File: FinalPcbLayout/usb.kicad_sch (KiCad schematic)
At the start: 1 part, among them J5 USB_C_Receptacle

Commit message: sound chip done
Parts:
- added R8, R9: 5.1k, symbol Device:R
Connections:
- net GND1: now reaches J5.A1 (GND), J5.A12 (GND), J5.B1 (GND), J5.B12 (GND)
- net VCC: now reaches J5.A4 (VBUS), J5.A9 (VBUS), J5.B4 (VBUS), J5.B9 (VBUS)
- net at J5.A5 (CC1): now also R9.1
- net D+1: now reaches J5.A6 (D+)
- net D+1: now also J5.B7 (D-)
- net D-1: now reaches J5.A7 (D-)
- net D-1: now also J5.B6 (D+)
- net at J5.B5 (CC2): now also R8.1
- net GND: now reaches J5.S1 (SHIELD)
- net GND: now also R8.2, R9.2
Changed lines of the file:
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@@
 (kicad_sch (version 20230121) (generator eeschema)
   (paper "A4")
+  (wire (pts (xy 157.48 68.58) (xy 209.55 68.58))
+    (stroke (width 0) (type default))
+  )
+  (wire (pts (xy 157.48 78.74) (xy 162.56 78.74))
+    (stroke (width 0) (type default))
+  )
+  (wire (pts (xy 209.55 68.58) (xy 209.55 69.85))
+    (stroke (width 0) (type default))
+  )
+  (wire (pts (xy 157.48 83.82) (xy 170.18 83.82))
+    (stroke (width 0) (type default))
+  )
+  (wire (pts (xy 162.56 81.28) (xy 157.48 81.28))
+    (stroke (width 0) (type default))
+  )
+  (wire (pts (xy 170.18 76.2) (xy 157.48 76.2))
+    (stroke (width 0) (type default))
+  )
+  (wire (pts (xy 170.18 83.82) (xy 170.18 76.2))
+    (stroke (width 0) (type default))
+  )
+  (wire (pts (xy 162.56 78.74) (xy 162.56 81.28))
+    (stroke (width 0) (type default))
+  )
+  (wire (pts (xy 157.48 71.12) (xy 187.96 71.12))
+    (stroke (width 0) (type default))
+  )
+  (hierarchical_label "D+1" (shape input) (at 162.56 81.28 0) (fields_autoplaced)
+    (effects (font (size 1.27 1.27)) (justify left))
+  )
+  (hierarchical_label "GND1" (shape input) (at 142.24 129.54 270) (fields_autoplaced)
+    (effects (font (size 1.27 1.27)) (justify right))
+  )
+  (hierarchical_label "VCC" (shape input) (at 157.48 63.5 0) (fields_autoplaced)
+    (effects (font (size 1.27 1.27)) (justify left))
+  )
+  (hierarchical_label "D-1" (shape input) (at 170.18 76.2 0) (fields_autoplaced)
+    (effects (font (size 1.27 1.27)) (justify left))
+  )
+  (symbol (lib_id "power:GND") (at 187.96 78.74 0) (unit 1)
+    (in_bom yes) (on_board yes) (dnp no) (fields_autoplaced)
+    (property "Reference" "#PWR027" (at 187.96 85.09 0)
+      (effects (font (size 1.27 1.27)) hide)
+    )
+    (property "Value" "GND" (at 187.96 83.82 0)
+      (effects (font (size 1.27 1.27)))
+    )
+    (property "Footprint" "" (at 187.96 78.74 0)
+      (effects (font (size 1.27 1.27)) hide)
+    )
+    (property "Datasheet" "" (at 187.96 78.74 0)
+      (effects (font (size 1.27 1.27)) hide)
+    )
+    (pin "1")
+    (instances
+      (project "FinalPcbLayout"
+        (path "/9fcc273e-b318-4ade-b4c7-fe4ddbf9d677/80fb5872-9ff7-41e5-9921-84d432e9852e"
+          (reference "#PWR027") (unit 1)
+        )
+      )
+    )
+  )
+  (symbol (lib_id "Device:R") (at 209.55 73.66 0) (unit 1)
+    (in_bom yes) (on_board yes) (dnp no) (fields_autoplaced)
+    (property "Reference" "R9" (at 212.09 72.39 0)
+      (effects (font (size 1.27 1.27)) (justify left))
+    )
+    (property "Value" "5.1k" (at 212.09 74.93 0)
+      (effects (font (size 1.27 1.27)) (justify left))
+    )
+    (property "Footprint" "" (at 207.772 73.66 90)
+      (effects (font (size 1.27 1.27)) hide)
+    )
+    (property "Datasheet" "~" (at 209.55 73.66 0)
+      (effects (font (size 1.27 1.27)) hide)
+    )
+    (pin "1")
+    (pin "2")
+    (instances
+      (project "FinalPcbLayout"
+        (path "/9fcc273e-b318-4ade-b4c7-fe4ddbf9d677/80fb5872-9ff7-41e5-9921-84d432e9852e"
+          (reference "R9") (unit 1)
+        )
+      )
+    )
+  )
+  (symbol (lib_id "power:GND") (at 209.55 77.47 0) (unit 1)
+    (in_bom yes) (on_board yes) (dnp no) (fields_autoplaced)
+    (property "Reference" "#PWR028" (at 209.55 83.82 0)
+      (effects (font (size 1.27 1.27)) hide)
+    )
+    (property "Value" "GND" (at 209.55 82.55 0)
+      (effects (font (size 1.27 1.27)))
+    )
+    (property "Footprint" "" (at 209.55 77.47 0)
+      (effects (font (size 1.27 1.27)) hide)
+    )
+    (property "Datasheet" "" (at 209.55 77.47 0)
+      (effects (font (size 1.27 1.27)) hide)
+    )
+    (pin "1")
+    (instances
+      (project "FinalPcbLayout"
+        (path "/9fcc273e-b318-4ade-b4c7-fe4ddbf9d677/80fb5872-9ff7-41e5-9921-84d432e9852e"
+          (reference "#PWR028") (unit 1)
+        )
+      )
+    )
+  )
+  (symbol (lib_id "power:GND") (at 134.62 129.54 0) (unit 1)
+    (in_bom yes) (on_board yes) (dnp no) (fields_autoplaced)
+    (property "Reference" "#PWR07" (at 134.62 135.89 0)
+      (effects (font (size 1.27 1.27)) hide)
+    )
+    (property "Value" "GND" (at 134.62 134.62 0)
+      (effects (font (size 1.27 1.27)))
+    )
+    (property "Footprint" "" (at 134.62 129.54 0)
+      (effects (font (size 1.27 1.27)) hide)
+    )
+    (property "Datasheet" "" (at 134.62 129.54 0)
+      (effects (font (size 1.27 1.27)) hide)
+    )
+    (pin "1")
+    (instances
+      (project "FinalPcbLayout"
+        (path "/9fcc273e-b318-4ade-b4c7-fe4ddbf9d677/80fb5872-9ff7-41e5-9921-84d432e9852e"
+          (reference "#PWR07") (unit 1)
+        )
+      )
+    )
+  )
+  (symbol (lib_id "Device:R") (at 187.96 74.93 0) (unit 1)
+    (in_bom yes) (on_board yes) (dnp no) (fields_autoplaced)
+    (property "Reference" "R8" (at 190.5 73.66 0)
+      (effects (font (size 1.27 1.27)) (justify left))
+    )
+    (property "Value" "5.1k" (at 190.5 76.2 0)
+      (effects (font (size 1.27 1.27)) (justify left))
+    )
+    (property "Footprint" "" (at 186.182 74.93 90)
+      (effects (font (size 1.27 1.27)) hide)
+    )
+    (property "Datasheet" "~" (at 187.96 74.93 0)
+      (effects (font (size 1.27 1.27)) hide)
+    )
+    (pin "1")
+    (pin "2")
+    (instances
+      (project "FinalPcbLayout"
+        (path "/9fcc273e-b318-4ade-b4c7-fe4ddbf9d677/80fb5872-9ff7-41e5-9921-84d432e9852e"
+          (reference "R8") (unit 1)
+        )
+      )
+    )
+  )
   (symbol (lib_id "Connector:USB_C_Receptacle") (at 142.24 88.9 0) (unit 1)
     (in_bom yes) (on_board yes) (dnp no) (fields_autoplaced)

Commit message: beep
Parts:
- added U6: CP2102N-Axx-xQFN28, Package_DFN_QFN:QFN-28-1EP_5x5mm_P0.5mm_EP3.35x3.35mm, symbol Interface_USB:CP2102N-Axx-xQFN28
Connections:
- new net: U6.29 (GND), U6.3 (GND)
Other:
- moved on the sheet: J5, R8, R9

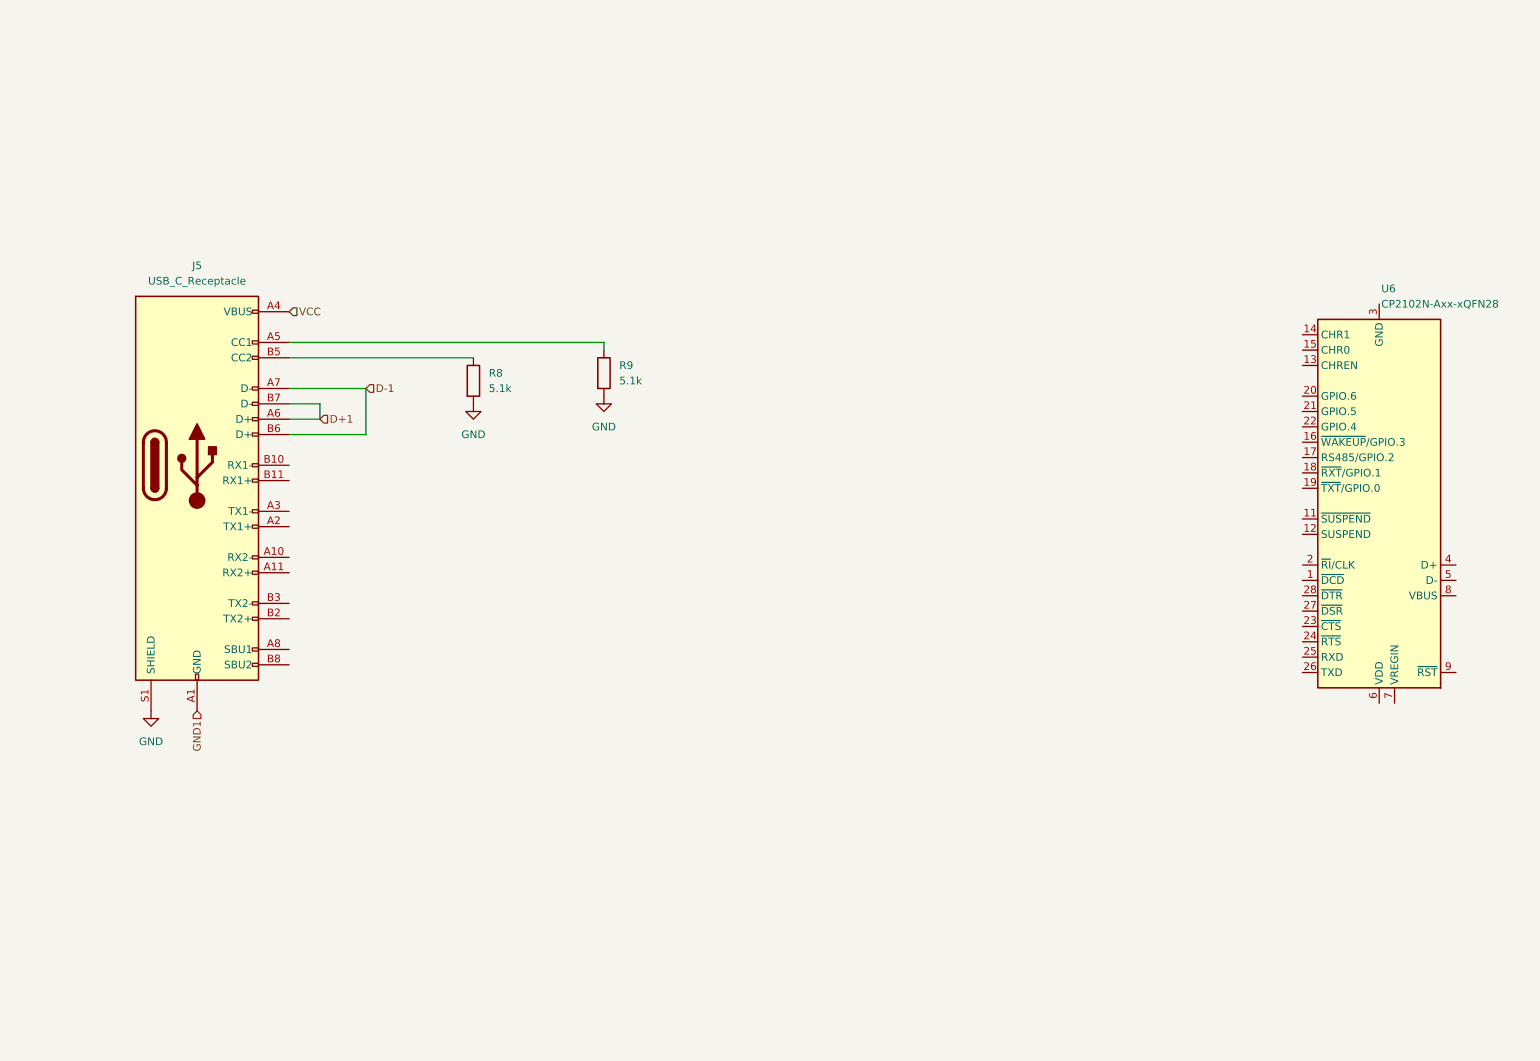
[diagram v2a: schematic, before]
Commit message: USB Autoprogramming
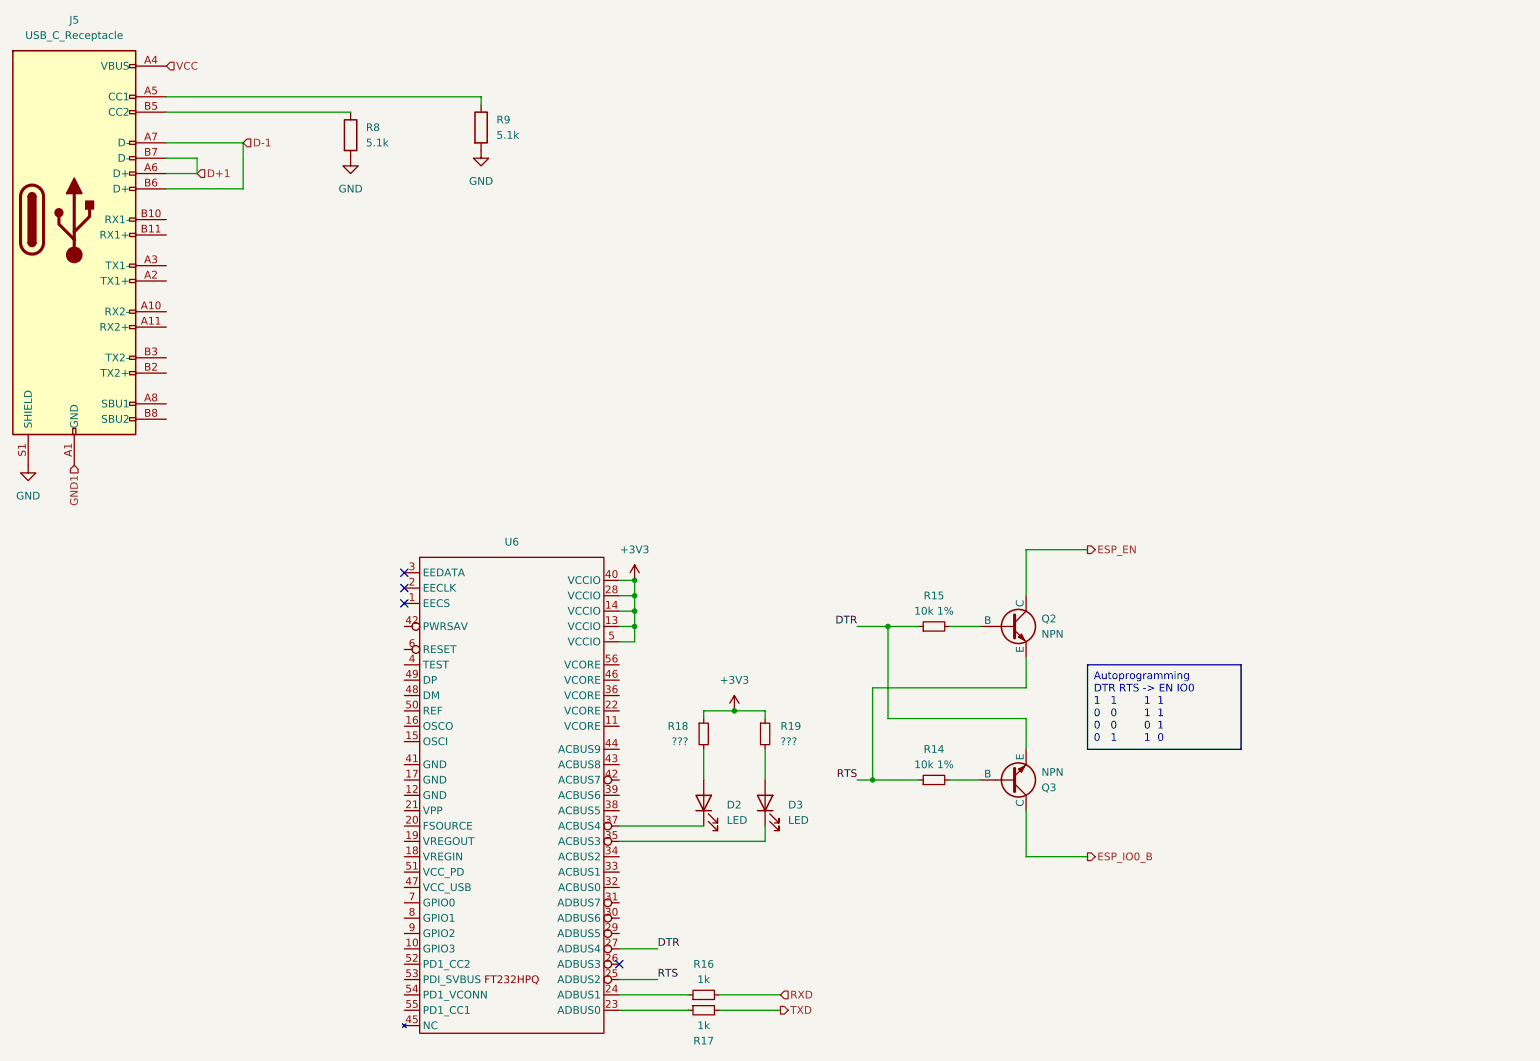
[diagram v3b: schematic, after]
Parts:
- removed U6: CP2102N-Axx-xQFN28, Package_DFN_QFN:QFN-28-1EP_5x5mm_P0.5mm_EP3.35x3.35mm, symbol Interface_USB:CP2102N-Axx-xQFN28
- added D2, D3: LED, symbol Device:LED
- added Q2, Q3: NPN, symbol Simulation_SPICE:NPN
- added R14, R15: 10k 1%, symbol Device:R_Small
- added R16, R17: 1k, symbol Device:R_Small
- added R18, R19: ???, symbol Device:R_Small
- added U6: ~, Package_DFN_QFN:QFN-56-1EP_8x8mm_P0.5mm_EP4.5x5.2mm_ThermalVias, symbol OSMI-parts:FT232HPQ
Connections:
- new net: D3.1 (K), U6.35 (ACBUS3)
- new net: D3.2 (A), R19.2
- new net: R17.1, U6.23 (ADBUS0)
- new net: D2.2 (A), R18.2
- new net: Q2.2 (B), R15.2
- new net: Q3.2 (B), R14.2
- new net: D2.1 (K), U6.37 (ACBUS4)
- new net: R16.1, U6.24 (ADBUS1)
- new net +3V3: R18.1, R19.1, U6.13 (VCCIO), U6.14 (VCCIO), U6.28 (VCCIO), U6.40 (VCCIO), U6.5 (VCCIO)
- new net DTR: Q3.3 (E), R15.1, U6.27 (ADBUS4)
- new net ESP_EN: Q2.1 (C)
- new net ESP_IO0_B: Q3.1 (C)
- new net RTS: Q2.3 (E), R14.1, U6.25 (ADBUS2)
- new net RXD: R16.2
- new net TXD: R17.2
- no-connect marks 0 -> 4
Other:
- moved on the sheet: J5, R8, R9

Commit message: VCORE Connections
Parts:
- added C20: 3.3u, symbol Device:C_Small
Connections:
- net GND: now also C20.2
- net +1V2: now reaches U6.11 (VCORE)
- net +1V2: now also U6.19 (VREGOUT), U6.22 (VCORE), U6.36 (VCORE), U6.46 (VCORE), U6.56 (VCORE), C20.1
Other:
- note added: "Update R to match forward i for D2 & D3"
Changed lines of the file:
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@@
 (kicad_sch (version 20230121) (generator eeschema)
   (paper "A4")
+  (junction (at 76.2 149.86) (diameter 0) (color 0 0 0 0)
+  )
+  (junction (at 132.08 123.19) (diameter 0) (color 0 0 0 0)
+  )
+  (junction (at 132.08 120.65) (diameter 0) (color 0 0 0 0)
+  )
   (junction (at 144.78 128.27) (diameter 0) (color 0 0 0 0)
   )
@@
   (junction (at 170.18 114.3) (diameter 0) (color 0 0 0 0)
   )
+  (junction (at 132.08 128.27) (diameter 0) (color 0 0 0 0)
+  )
   (junction (at 128.27 114.3) (diameter 0) (color 0 0 0 0)
+  )
+  (junction (at 132.08 125.73) (diameter 0) (color 0 0 0 0)
   )
   (junction (at 128.27 109.22) (diameter 0) (color 0 0 0 0)
@@
     (stroke (width 0) (type default))
   )
+  (wire (pts (xy 125.73 123.19) (xy 132.08 123.19))
+    (stroke (width 0) (type default))
+  )
+  (wire (pts (xy 125.73 125.73) (xy 132.08 125.73))
+    (stroke (width 0) (type default))
+  )
+  (wire (pts (xy 132.08 130.81) (xy 125.73 130.81))
+    (stroke (width 0) (type default))
+  )
   (wire (pts (xy 125.73 175.26) (xy 137.16 175.26))
     (stroke (width 0) (type default))
@@
     (stroke (width 0) (type default))
   )
+  (wire (pts (xy 76.2 149.86) (xy 90.17 149.86))
+    (stroke (width 0) (type default))
+  )
   (wire (pts (xy 125.73 149.86) (xy 149.86 149.86))
     (stroke (width 0) (type default))
@@
     (stroke (width 0) (type default))
   )
+  (wire (pts (xy 125.73 120.65) (xy 132.08 120.65))
+    (stroke (width 0) (type default))
+  )
   (wire (pts (xy 165.1 114.3) (xy 170.18 114.3))
     (stroke (width 0) (type default))
@@
     (stroke (width 0) (type default))
   )
+  (wire (pts (xy 125.73 128.27) (xy 132.08 128.27))
+    (stroke (width 0) (type default))
+  )
+  (wire (pts (xy 132.08 123.19) (xy 132.08 120.65))
+    (stroke (width 0) (type default))
+  )
   (wire (pts (xy 55.88 39.37) (xy 50.8 39.37))
     (stroke (width 0) (type default))
@@
     (stroke (width 0) (type default))
   )
+  (wire (pts (xy 132.08 125.73) (xy 132.08 128.27))
+    (stroke (width 0) (type default))
+  )
   (wire (pts (xy 180.34 114.3) (xy 185.42 114.3))
     (stroke (width 0) (type default))
@@
   )
   (wire (pts (xy 125.73 111.76) (xy 128.27 111.76))
+    (stroke (width 0) (type default))
+  )
+  (wire (pts (xy 132.08 128.27) (xy 132.08 130.81))
+    (stroke (width 0) (type default))
+  )
+  (wire (pts (xy 132.08 123.19) (xy 132.08 125.73))
     (stroke (width 0) (type default))
   )
@@
     (fill (type none))
     (effects (font (size 1.27 1.27)) (justify left top))
+  )
+  (text "Update R to match forward i\nfor D2 & D3" (at 130.81 139.7 0)
+    (effects (font (size 1.27 1.27)) (justify left bottom))
   )
   (label "DTR" (at 132.08 167.64 0) (fields_autoplaced)
@@
     )
   )
+  (symbol (lib_id "power:GND") (at 76.2 154.94 0) (unit 1)
+    (in_bom yes) (on_board yes) (dnp no) (fields_autoplaced)
+    (property "Reference" "#PWR040" (at 76.2 161.29 0)
+      (effects (font (size 1.27 1.27)) hide)
+    )
+    (property "Value" "GND" (at 76.2 160.02 0)
+      (effects (font (size 1.27 1.27)))
+    )
+    (property "Footprint" "" (at 76.2 154.94 0)
+      (effects (font (size 1.27 1.27)) hide)
+    )
+    (property "Datasheet" "" (at 76.2 154.94 0)
+      (effects (font (size 1.27 1.27)) hide)
+    )
+    (pin "1")
+    (instances
+      (project "FinalPcbLayout"
+        (path "/9fcc273e-b318-4ade-b4c7-fe4ddbf9d677/80fb5872-9ff7-41e5-9921-84d432e9852e"
+          (reference "#PWR040") (unit 1)
+        )
+      )
+    )
+  )
   (symbol (lib_id "power:GND") (at 102.87 35.56 0) (unit 1)
     (in_bom yes) (on_board yes) (dnp no) (fields_autoplaced)
@@
         (path "/9fcc273e-b318-4ade-b4c7-fe4ddbf9d677/80fb5872-9ff7-41e5-9921-84d432e9852e"
           (reference "#PWR07") (unit 1)
+        )
+      )
+    )
+  )
+  (symbol (lib_id "Device:C_Small") (at 76.2 152.4 0) (unit 1)
+    (in_bom yes) (on_board yes) (dnp no)
+    (property "Reference" "C20" (at 73.66 151.1363 0)
+      (effects (font (size 1.27 1.27)) (justify right))
+    )
+    (property "Value" "3.3u" (at 73.66 153.6763 0)
+      (effects (font (size 1.27 1.27)) (justify right))
+    )
+    (property "Footprint" "" (at 76.2 152.4 0)
+      (effects (font (size 1.27 1.27)) hide)
+    )
+    (property "Datasheet" "~" (at 76.2 152.4 0)
+      (effects (font (size 1.27 1.27)) hide)
+    )
+    (pin "1")
+    (pin "2")
+    (instances
+      (project "FinalPcbLayout"
+        (path "/9fcc273e-b318-4ade-b4c7-fe4ddbf9d677/80fb5872-9ff7-41e5-9921-84d432e9852e"
+          (reference "C20") (unit 1)
         )
       )
@@
         (path "/9fcc273e-b318-4ade-b4c7-fe4ddbf9d677/80fb5872-9ff7-41e5-9921-84d432e9852e"
           (reference "Q3") (unit 1)
+        )
+      )
+    )
+  )
+  (symbol (lib_id "power:+1V2") (at 76.2 149.86 0) (unit 1)
+    (in_bom yes) (on_board yes) (dnp no) (fields_autoplaced)
+    (property "Reference" "#PWR039" (at 76.2 153.67 0)
+      (effects (font (size 1.27 1.27)) hide)
+    )
+    (property "Value" "+1V2" (at 76.2 144.78 0)
+      (effects (font (size 1.27 1.27)))
+    )
+    (property "Footprint" "" (at 76.2 149.86 0)
+      (effects (font (size 1.27 1.27)) hide)
+    )
+    (property "Datasheet" "" (at 76.2 149.86 0)
+      (effects (font (size 1.27 1.27)) hide)
+    )
+    (pin "1")
+    (instances
+      (project "FinalPcbLayout"
+        (path "/9fcc273e-b318-4ade-b4c7-fe4ddbf9d677/80fb5872-9ff7-41e5-9921-84d432e9852e"
+          (reference "#PWR039") (unit 1)
         )
       )
@@
         )
       )
+    )
+  )
+  (symbol (lib_id "power:+1V2") (at 132.08 120.65 0) (unit 1)
+    (in_bom yes) (on_board yes) (dnp no) (fields_autoplaced)
+    (property "Reference" "#PWR041" (at 132.08 124.46 0)
+      (effects (font (size 1.27 1.27)) hide)
+    )
+    (property "Value" "+1V2" (at 132.08 115.57 0)
+      (effects (font (size 1.27 1.27)))
+    )
+    (property "Footprint" "" (at 132.08 120.65 0)
+      (effects (font (size 1.27 1.27)) hide)
+    )
+    (property "Datasheet" "" (at 132.08 120.65 0)
+      (effects (font (size 1.27 1.27)) hide)
+    )
+    (pin "1")
+    (instances
+      (project "FinalPcbLayout"
+        (path "/9fcc273e-b318-4ade-b4c7-fe4ddbf9d677/80fb5872-9ff7-41e5-9921-84d432e9852e"
+          (reference "#PWR041") (unit 1)
+        )
+      )
